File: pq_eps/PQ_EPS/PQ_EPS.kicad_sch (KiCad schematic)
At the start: 88 parts, among them IC1 DS2782E+, IC2 ISL9120IRTNZ, J1 CES-110-02-L-S, J2 CES-110-02-L-S, J3 CES-110-02-L-S, J4 CES-110-02-L-S, Q1 SIR424DP, U1 SPV1040TTR, U2 SPV1040TTR, U3 SPV1040TTR, U4 LTC4040EUFD#PBF

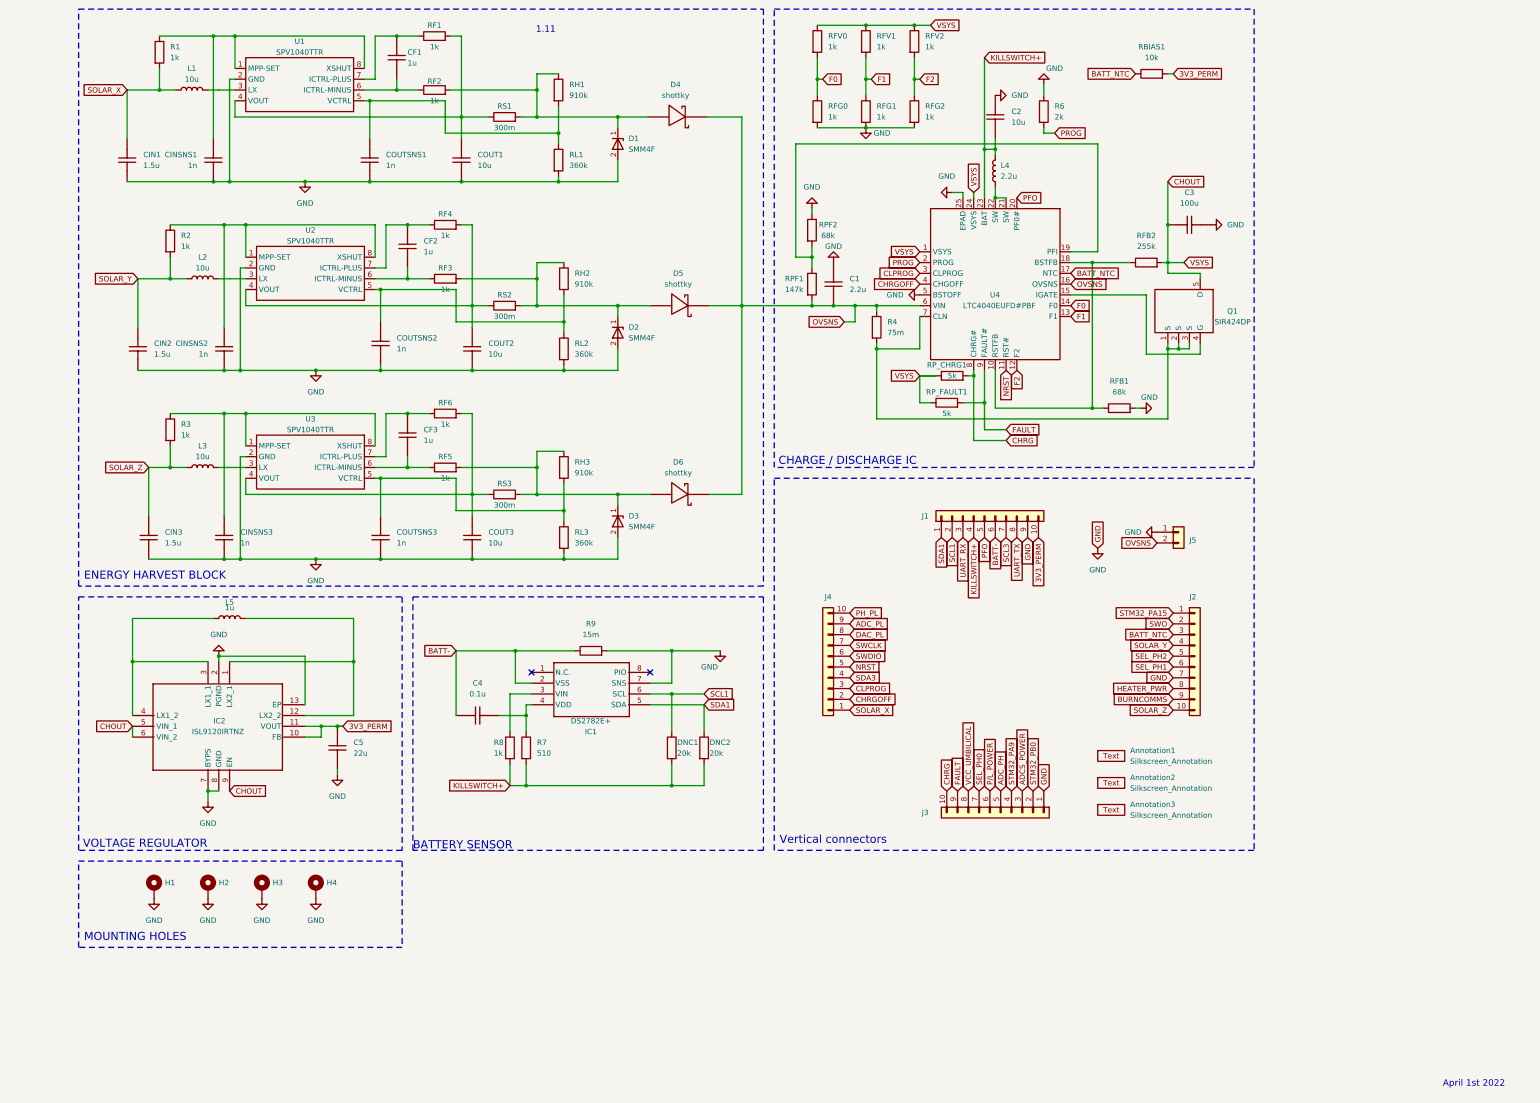
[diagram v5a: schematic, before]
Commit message: EPS changes in progress. Will change to a new implementation
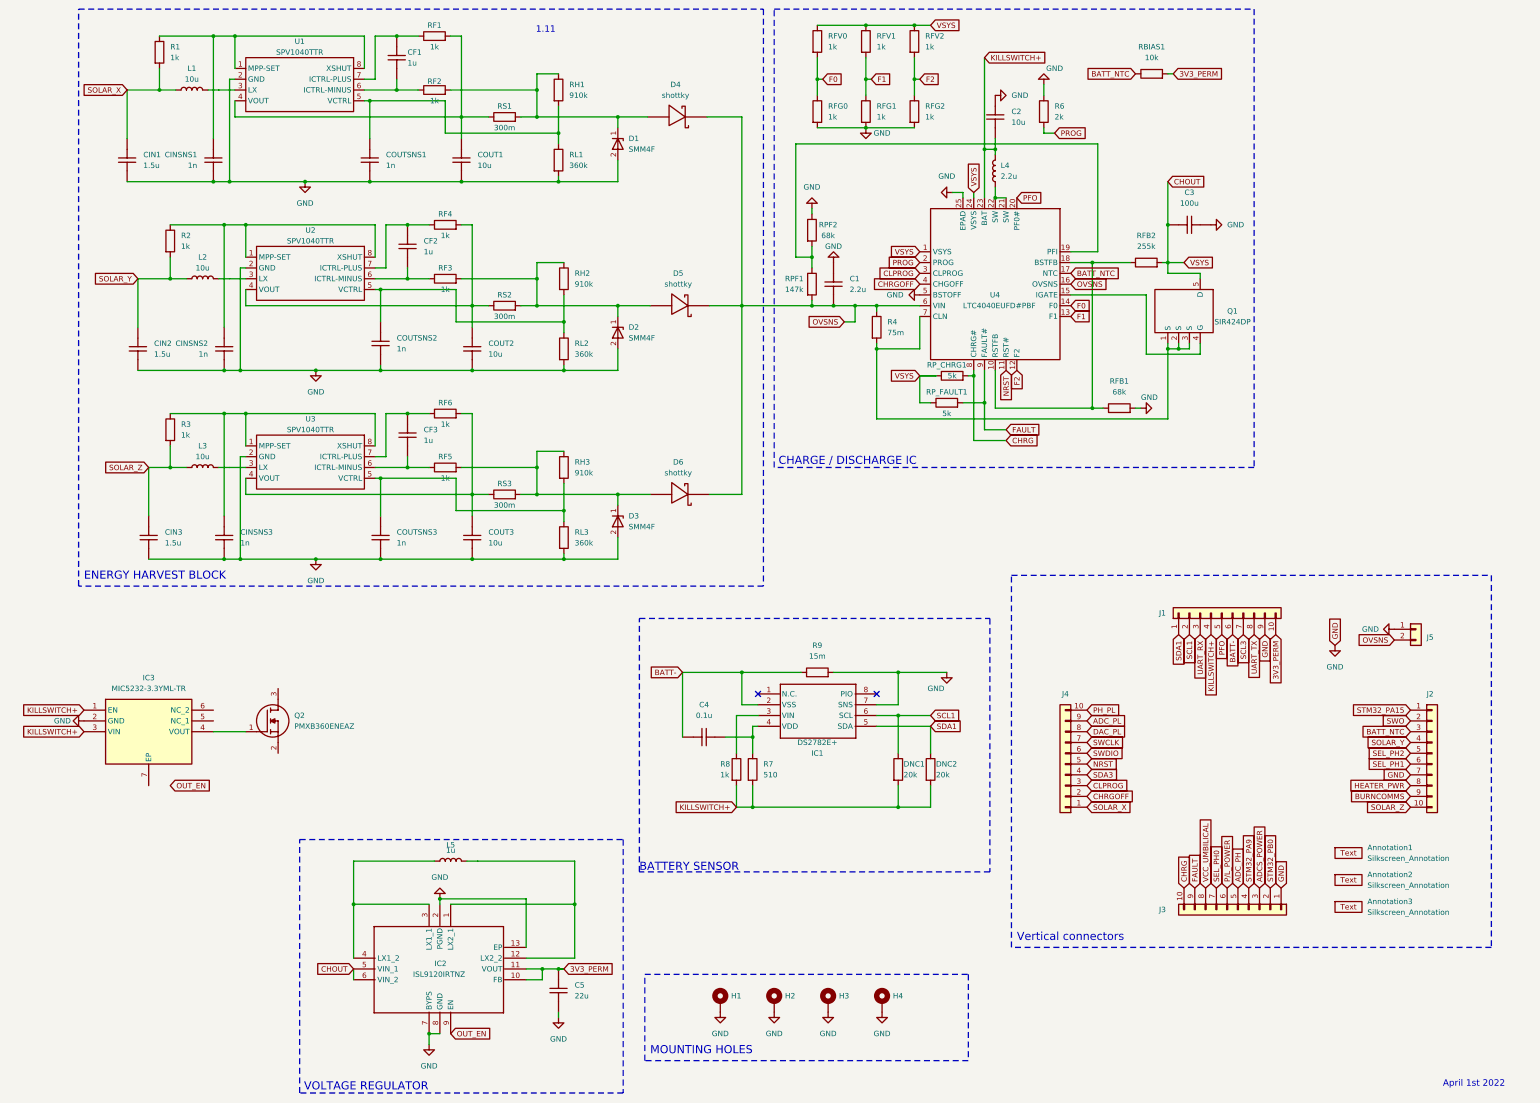
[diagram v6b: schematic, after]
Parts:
- added IC3: MIC5232-3.3YML-TR, SON65P200X200X95-7N-D, symbol MIC5232-3_3YML-TR:MIC5232-3.3YML-TR
- added Q2: PMXB360ENEAZ, PMXB360ENEAZ, symbol PMXB360ENEAZ:PMXB360ENEAZ
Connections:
- net CHOUT: no longer IC2.9 (EN)
- net GND: now also IC3.2 (GND)
- net KILLSWITCH+: now also IC3.1 (EN), IC3.3 (VIN)
- new net: IC3.4 (VOUT), Q2.1 (G)
- new net OUT_EN: IC2.9 (EN)
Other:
- moved on the sheet: Annotation1, Annotation2, Annotation3, C4, C5, DNC1, DNC2, H1, H2, H3, H4, IC1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

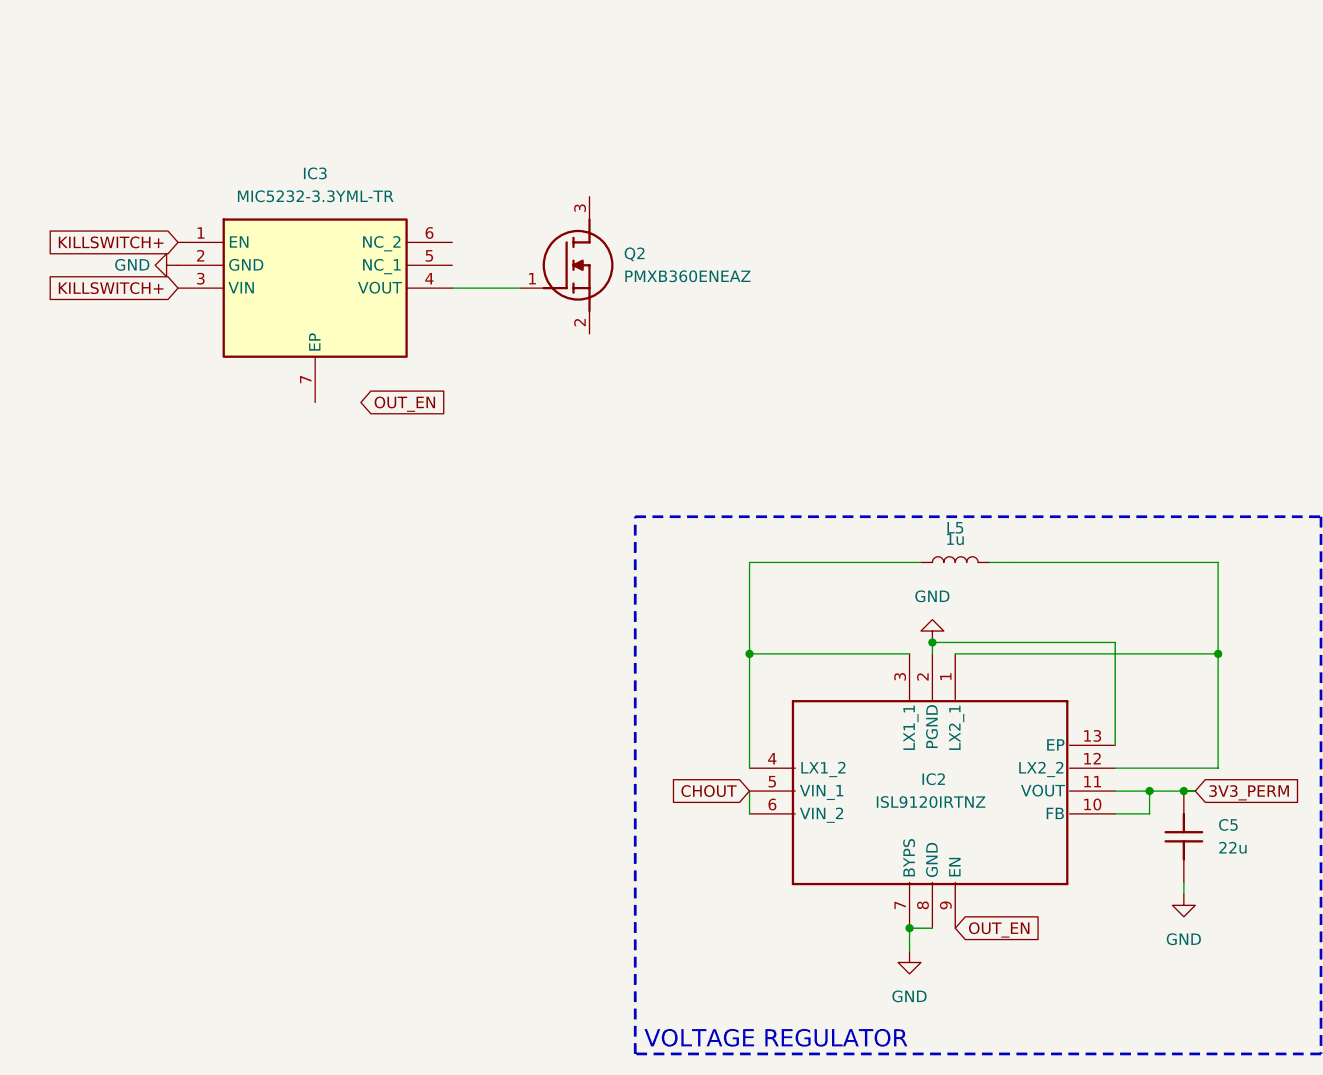
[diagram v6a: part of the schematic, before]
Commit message: EPS Changes done. Voltage Regulator ENABLED by Killswitch+
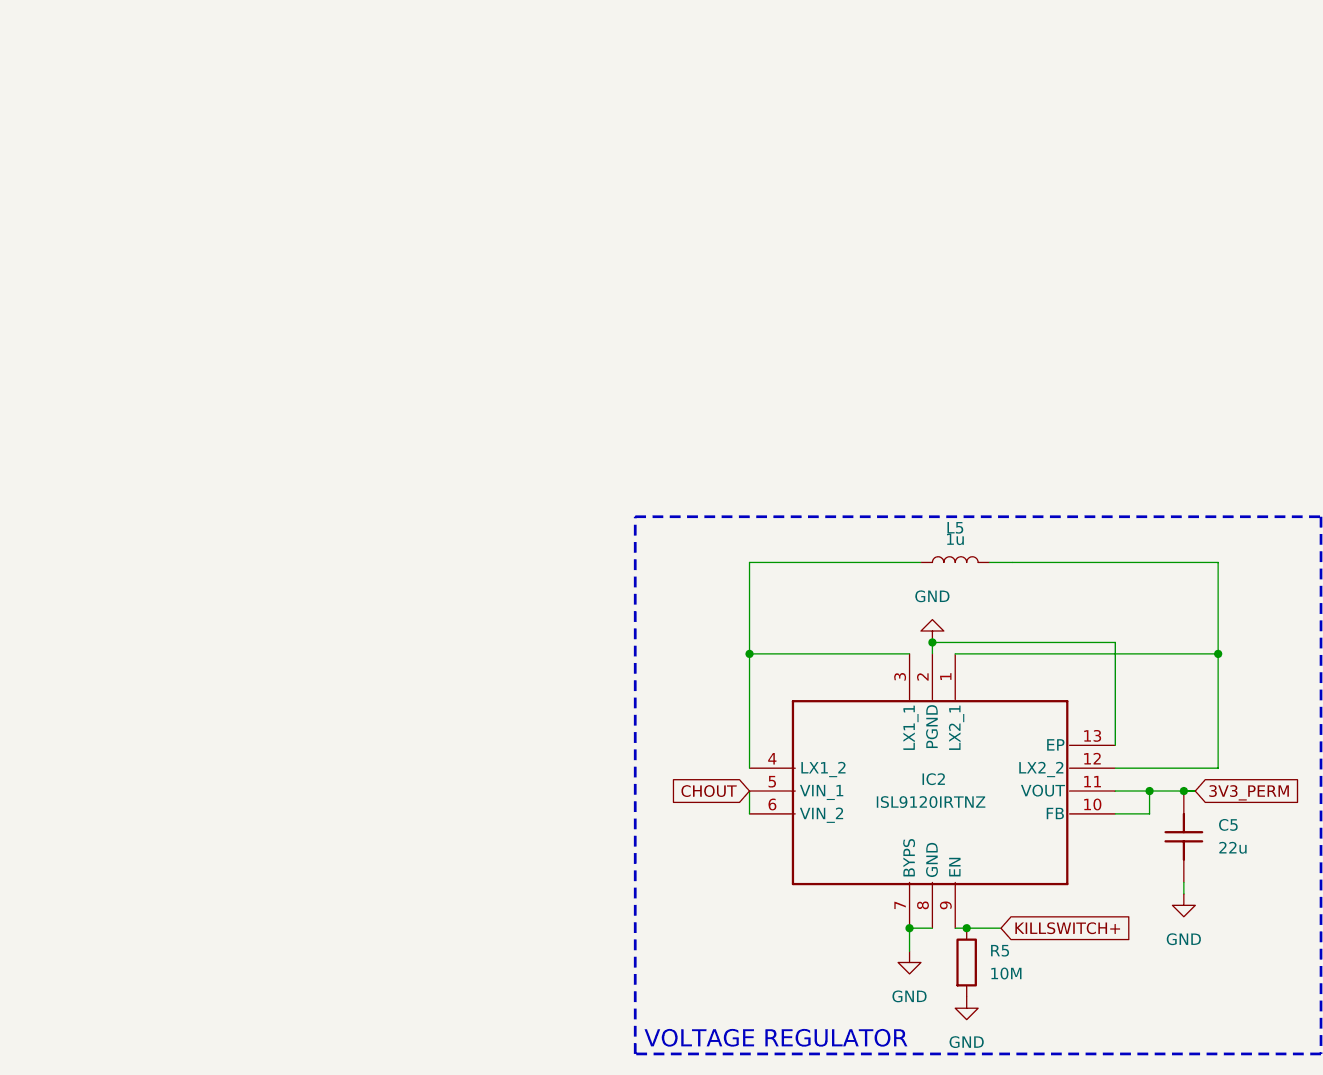
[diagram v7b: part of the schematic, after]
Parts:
- removed IC3: MIC5232-3.3YML-TR, SON65P200X200X95-7N-D, symbol MIC5232-3_3YML-TR:MIC5232-3.3YML-TR
- removed Q2: PMXB360ENEAZ, PMXB360ENEAZ, symbol PMXB360ENEAZ:PMXB360ENEAZ
- added R5: 10M, Resistor_SMD:R_0805_2012Metric, symbol Device:R
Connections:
- net OUT_EN is gone; now on net KILLSWITCH+: IC2.9 (EN)
- net GND: now also R5.2
- net KILLSWITCH+: now also R5.1
